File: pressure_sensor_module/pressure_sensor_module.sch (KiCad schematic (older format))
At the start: 9 parts, among them J1 Conn_02x04_Odd_Even, J2 Conn_02x07_Odd_Even, U1 MPX5100AP, U2 LM358

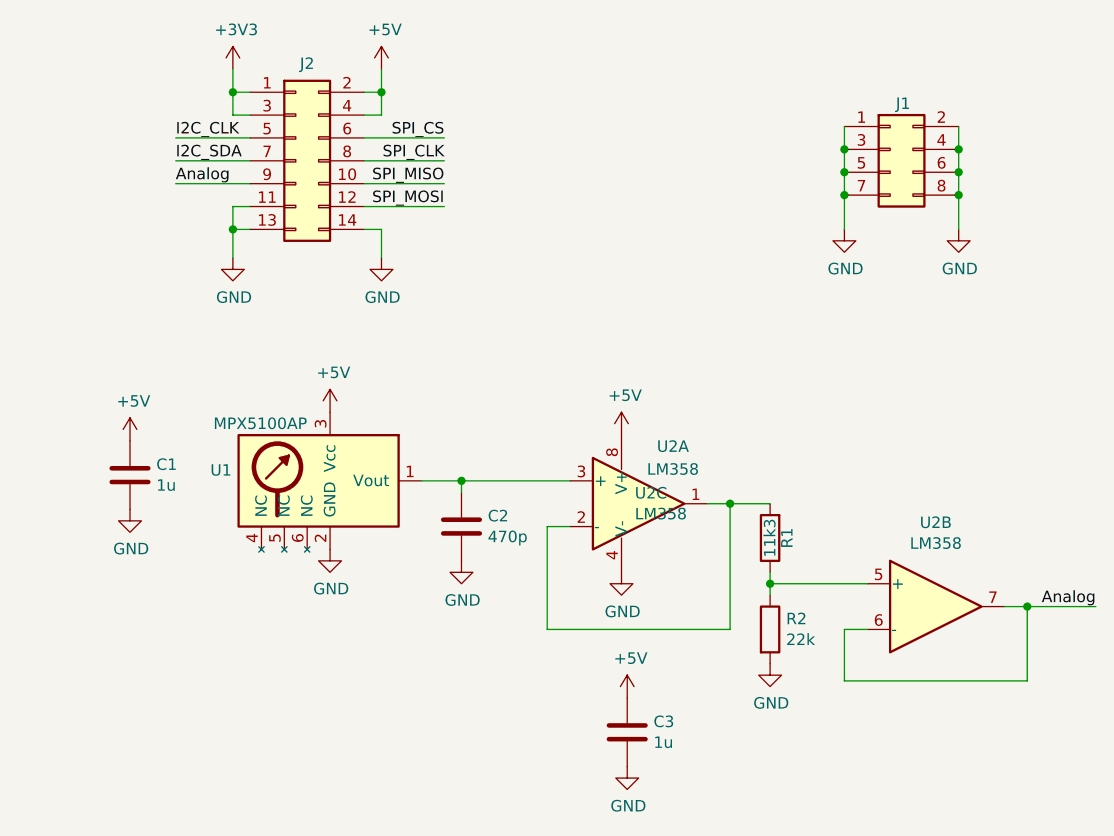
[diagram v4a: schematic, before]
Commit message: Added all references on silkscreen added BOM for sensor modules
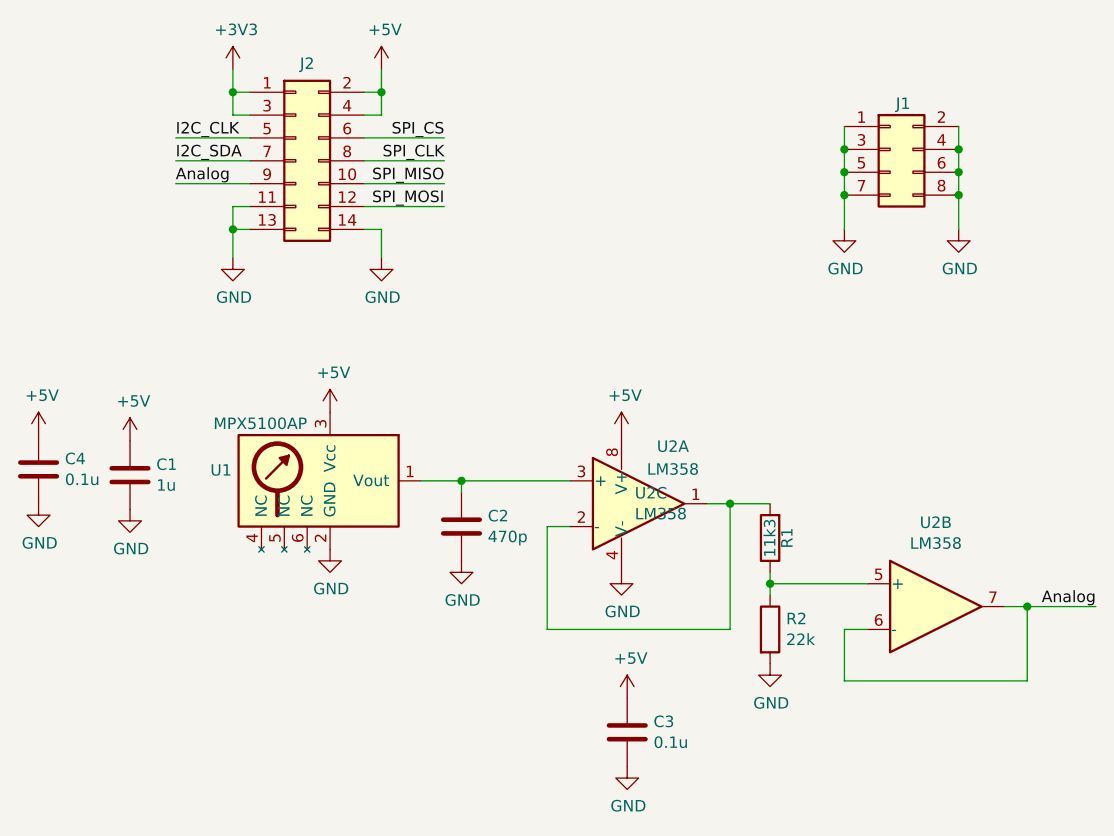
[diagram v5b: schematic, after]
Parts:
- added C4: 0.1u, Capacitor_SMD:C_0603_1608Metric, symbol Device:C
- C2: DigiKey (none) -> 1276-1168-1-ND
- C3: value 1u -> 0.1u; DigiKey 1276-1182-1-ND -> 1276-1258-1-ND
- J1: DigiKey (none) -> 609-6367-ND
- J2: DigiKey (none) -> 609-6365-ND
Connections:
- net +5V: now also C4.1
- net GND: now also C4.2
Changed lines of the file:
@@
 F 2 "Connector_PinHeader_2.54mm:PinHeader_2x04_P2.54mm_Vertical_SMD" H 4950 1825 50  0001 C CNN
 F 3 "~" H 4950 1825 50  0001 C CNN
+F 4 "609-6367-ND" H 4950 1825 50  0001 C CNN "DigiKey"
 	1    4950 1825
 	1    0    0    -1
@@
 F 2 "Connector_PinHeader_2.54mm:PinHeader_2x07_P2.54mm_Vertical_SMD" H 2350 1875 50  0001 C CNN
 F 3 "~" H 2350 1875 50  0001 C CNN
+F 4 "609-6365-ND" H 2350 1875 50  0001 C CNN "DigiKey"
 	1    2350 1875
 	1    0    0    -1
@@
 F 2 "Capacitor_SMD:C_0603_1608Metric" H 3113 3325 50  0001 C CNN
 F 3 "~" H 3075 3475 50  0001 C CNN
+F 4 "1276-1168-1-ND" H 3075 3475 50  0001 C CNN "DigiKey"
 	1    3075 3475
 	1    0    0    -1
@@
 P 3800 4375
 F 0 "C3" H 3915 4421 50  0000 L CNN
-F 1 "1u" H 3915 4330 50  0000 L CNN
+F 1 "0.1u" H 3915 4330 50  0000 L CNN
 F 2 "Capacitor_SMD:C_0603_1608Metric" H 3838 4225 50  0001 C CNN
 F 3 "~" H 3800 4375 50  0001 C CNN
-F 4 "1276-1182-1-ND" H 3800 4375 50  0001 C CNN "DigiKey"
+F 4 "1276-1258-1-ND" H 3800 4375 50  0001 C CNN "DigiKey"
 	1    3800 4375
 	1    0    0    -1
@@
 	1    0    0    -1
 $EndComp
+$Comp
+L Device:C C4
+U 1 1 5F0A59F0
+P 1225 3225
+F 0 "C4" H 1340 3271 50  0000 L CNN
+F 1 "0.1u" H 1340 3180 50  0000 L CNN
+F 2 "Capacitor_SMD:C_0603_1608Metric" H 1263 3075 50  0001 C CNN
+F 3 "~" H 1225 3225 50  0001 C CNN
+F 4 "1276-1258-1-ND" H 1225 3225 50  0001 C CNN "DigiKey"
+	1    1225 3225
+	1    0    0    -1
+$EndComp
+$Comp
+L power:+5V #PWR017
+U 1 1 5F0A59FA
+P 1225 3075
+F 0 "#PWR017" H 1225 2925 50  0001 C CNN
+F 1 "+5V" H 1240 3248 50  0000 C CNN
+F 2 "" H 1225 3075 50  0001 C CNN
+F 3 "" H 1225 3075 50  0001 C CNN
+	1    1225 3075
+	1    0    0    -1
+$EndComp
+$Comp
+L power:GND #PWR018
+U 1 1 5F0A5A04
+P 1225 3375
+F 0 "#PWR018" H 1225 3125 50  0001 C CNN
+F 1 "GND" H 1230 3202 50  0000 C CNN
+F 2 "" H 1225 3375 50  0001 C CNN
+F 3 "" H 1225 3375 50  0001 C CNN
+	1    1225 3375
+	1    0    0    -1
+$EndComp
